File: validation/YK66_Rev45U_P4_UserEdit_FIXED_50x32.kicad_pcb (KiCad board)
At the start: 2 copper layers, 50 x 32 mm, 13 parts, among them J1 PHOENIX_1711725_2P_5p08

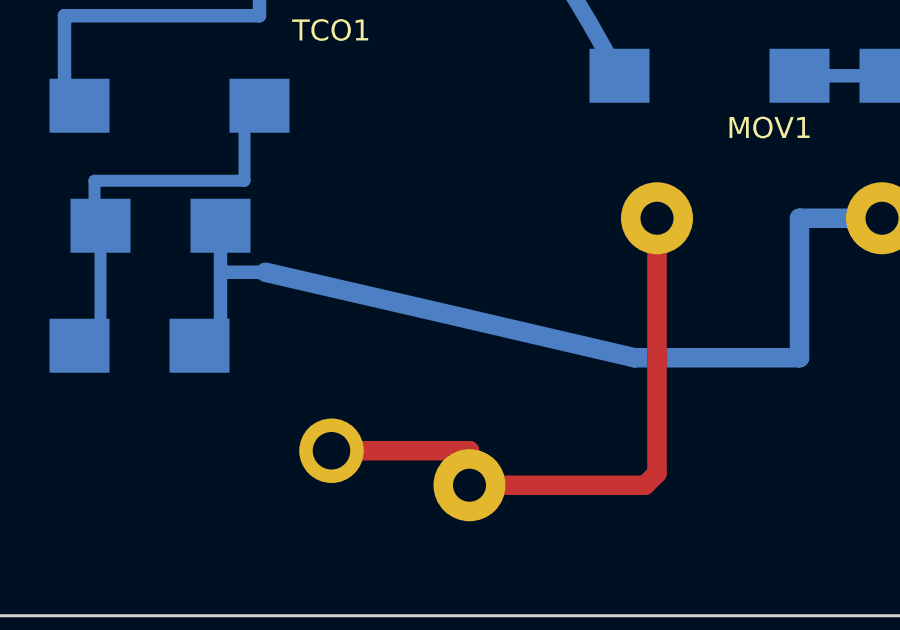
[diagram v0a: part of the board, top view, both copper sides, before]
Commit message: Fix malformed N copper arc causing PTH hole clearance violations; preserve routing endpoints
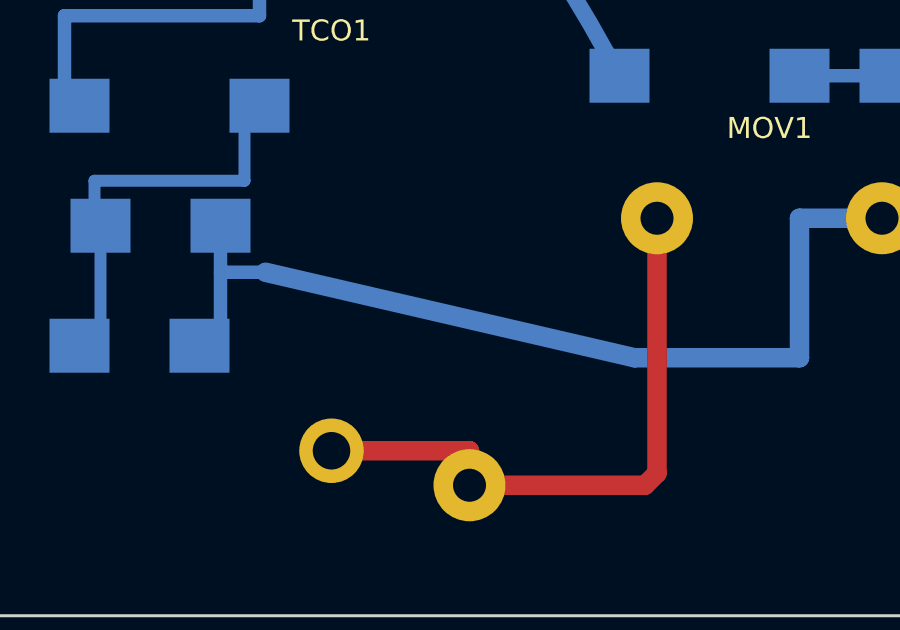
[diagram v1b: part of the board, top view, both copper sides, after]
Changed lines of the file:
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@@
 		(net 4)
 	)
-	(arc
+	(segment
 		(start 21.5000 23.4000)
-		(mid 15.7000 22.0500)
 		(end 9.2000 20.5500)
 		(width 0.650)
